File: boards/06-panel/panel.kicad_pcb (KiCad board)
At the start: 2 copper layers, 187 x 219 mm, 229 parts, among them J1 BUS, Q1 2N7000, Q10 2N7000, Q11 2N7000, Q12 2N7000, Q13 2N7000, Q14 2N7000, Q15 2N7000, Q16 2N7000, Q17 2N7000, Q18 2N7000, Q19 2N7000, Q2 2N7000, Q20 2N7000, Q21 2N7000, Q22 2N7000, Q23 2N7000, Q24 2N7000, Q25 2N7000, Q26 2N7000, Q27 2N7000, Q28 2N7000, Q29 2N7000, Q3 2N7000, Q30 2N7000, Q31 2N7000, Q32 2N7000, Q33 2N7000, Q34 2N7000, Q35 2N7000, Q36 2N7000, Q37 2N7000, Q38 2N7000, Q39 2N7000, Q4 2N7000, Q40 2N7000, Q41 2N7000, Q42 2N7000, Q43 2N7000, Q44 2N7000, Q45 2N7000, Q46 2N7000, Q47 2N7000, Q48 2N7000, Q49 2N7000, Q5 2N7000, Q50 2N7000, Q6 2N7000, Q7 2N7000, Q8 2N7000, Q9 2N7000, SW1 A3..A0 B3..B0, SW2 SUB EO AI AO BI BA AB OI, SW3 IO II PCE PCL FI HLT - -, SW4 DATA (closed = 1 on the bus), SW5 CLK, SW6 RST

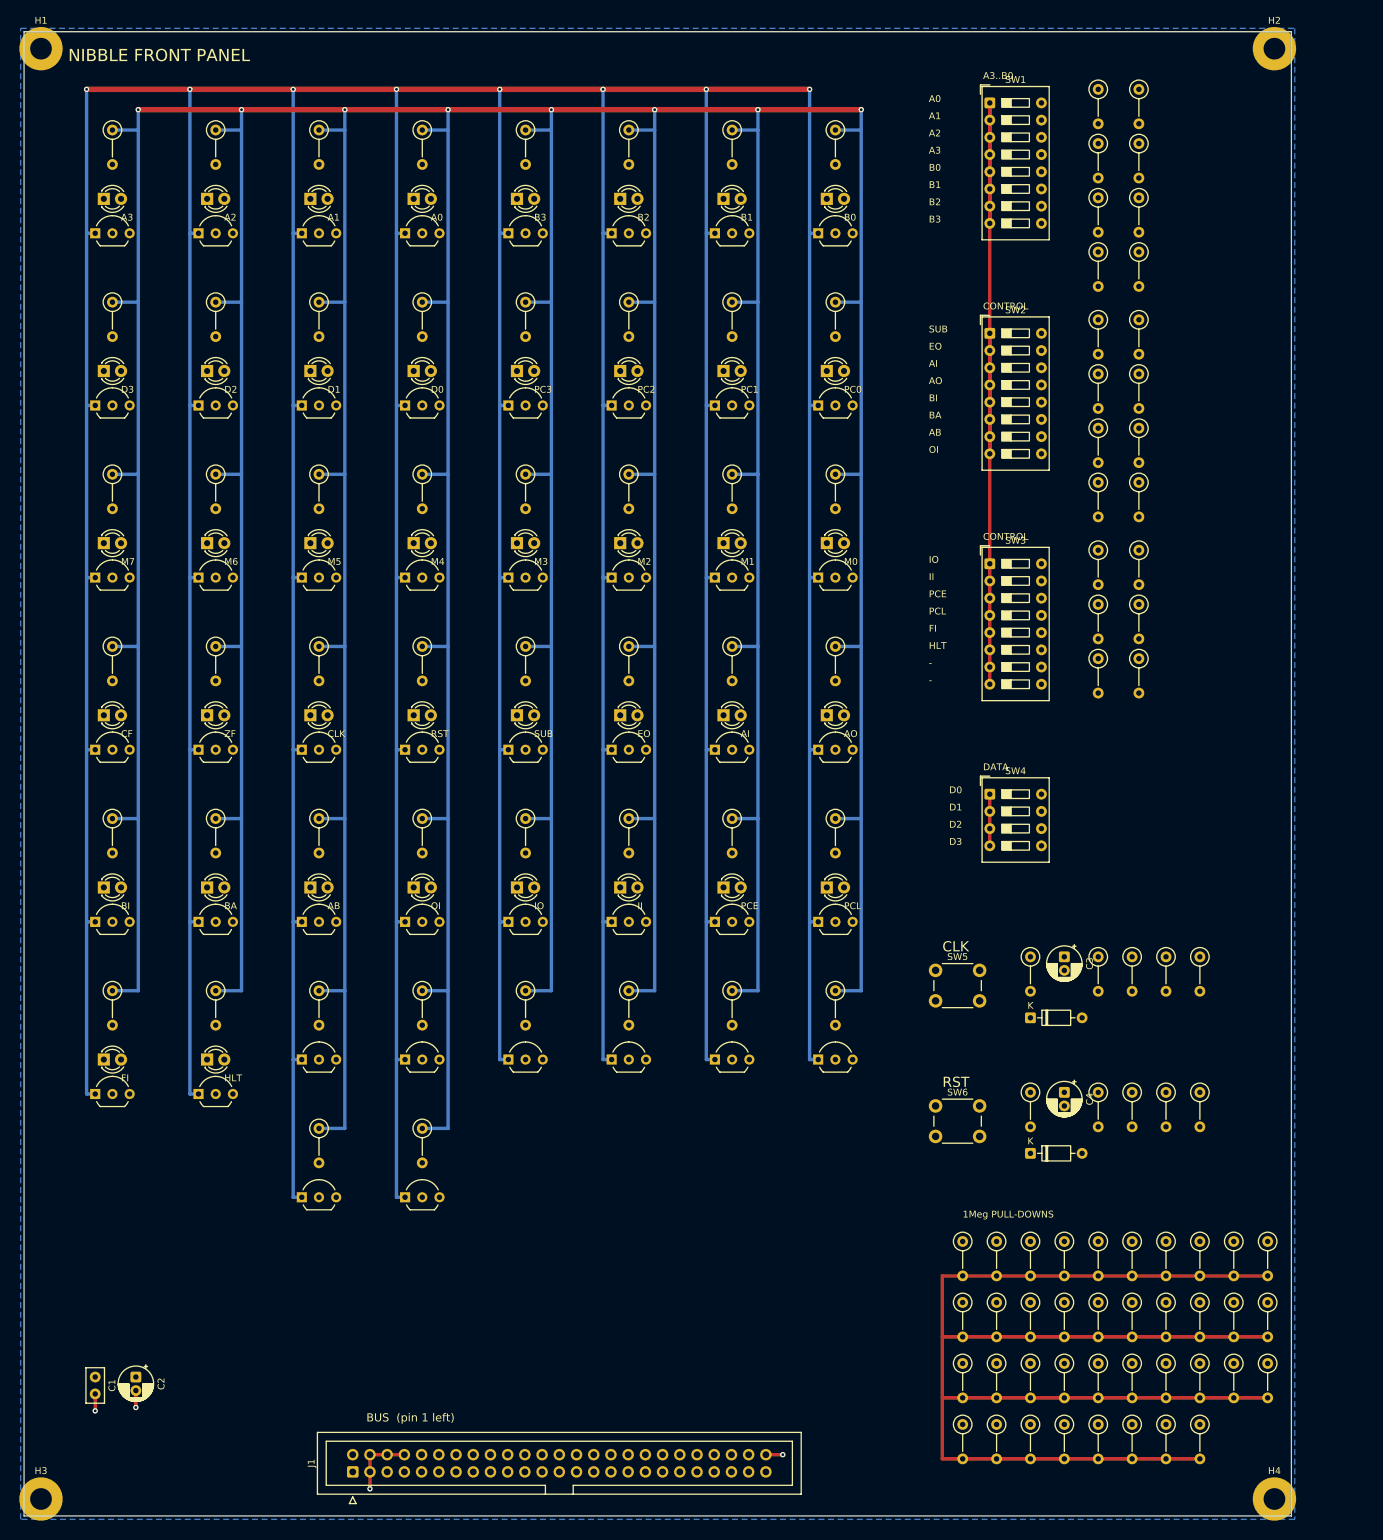
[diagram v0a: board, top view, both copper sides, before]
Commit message: Front panel PCB routed and DRC clean; all four order-1 boards complete
Panel 200x222 mm: LED rows labelled A3..B0 / D3..PC0 / M7..M0 / flags+control,
DIP switches with silk labels, CLK/RST buttons, pull-down grid, header at the
bottom. pcb.py: pre-routed power fixed in the DSN, keep-best across attempts,
DRC-verified ground stitching. Decision D016.

Co-Authored-By: Claude Fable 5.1 <noreply@anthropic.com>
Claude-Session: https://claude.ai/code/session_019vcbW37ERmrjZaWq55Er3J
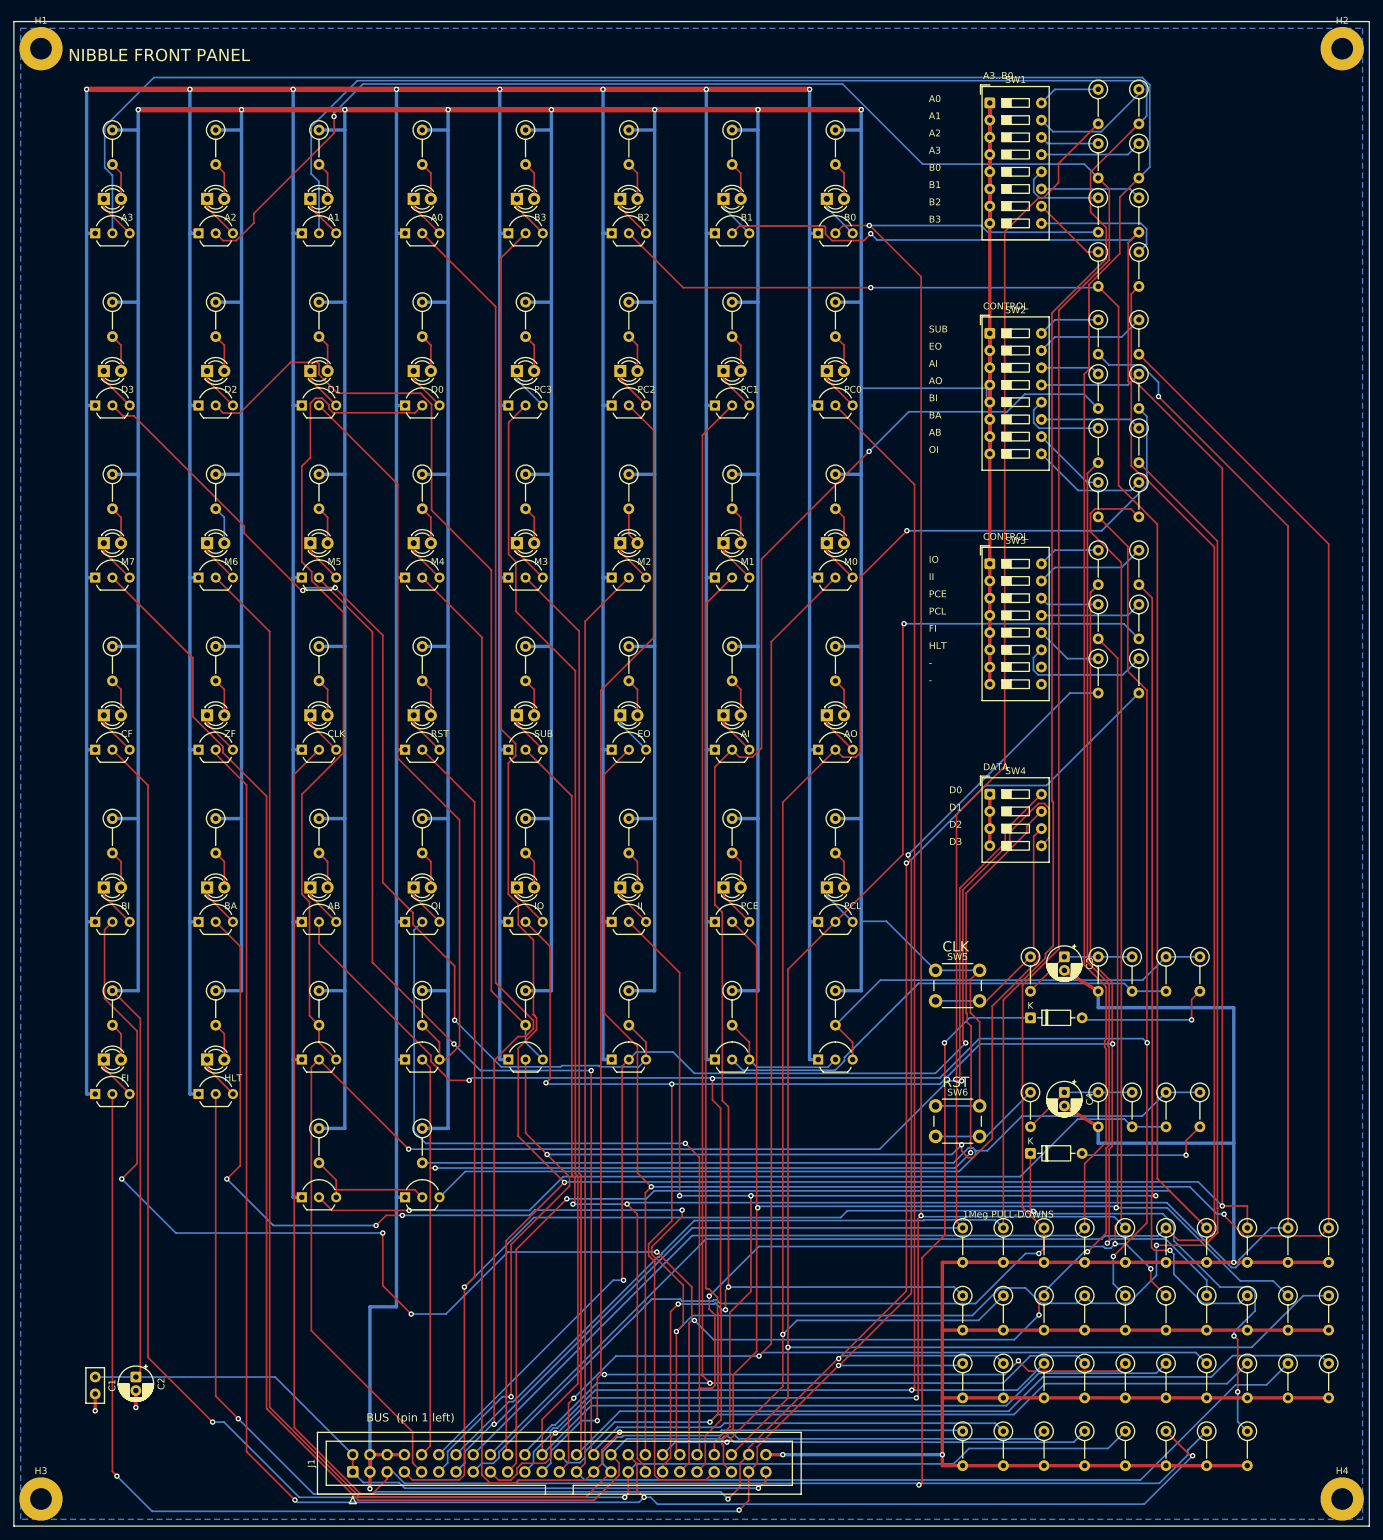
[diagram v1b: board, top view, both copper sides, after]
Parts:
- moved H2 10.0 mm to (196.0, 4.00)
- moved H4 10.0 mm to (196.0, 218.0)
- moved R42 9.22 mm to (194.0, 178.0)
- moved R52 9.06 mm to (194.0, 188.0)
- moved R62 9.00 mm to (194.0, 198.0)
- moved R41 8.25 mm to (188.0, 178.0)
- moved R51 8.06 mm to (188.0, 188.0)
- moved R61 8.00 mm to (188.0, 198.0)
- moved R40 7.28 mm to (182.0, 178.0)
- moved R50 7.07 mm to (182.0, 188.0)
- moved R70 7.07 mm to (182.0, 208.0)
- moved R60 7.00 mm to (182.0, 198.0)
- moved R39 6.32 mm to (176.0, 178.0)
- moved R49 6.08 mm to (176.0, 188.0)
- moved R69 6.08 mm to (176.0, 208.0)
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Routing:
- net A3: track 0.00 -> 453.4 mm
- net A0: track 0.00 -> 448.6 mm, vias 0 -> 1
- net B3: track 0.00 -> 439.9 mm, vias 0 -> 2
- net A1: track 0.00 -> 417.8 mm
- net A2: track 0.00 -> 412.9 mm, vias 0 -> 2
- net SUB: track 0.00 -> 366.5 mm, vias 0 -> 3
- net BA: track 0.00 -> 361.5 mm, vias 0 -> 6
- net B2: track 0.00 -> 359.3 mm, vias 0 -> 2
- net BI: track 0.00 -> 358.6 mm, vias 0 -> 7
- net EO: track 0.00 -> 352.8 mm, vias 0 -> 2
- net B1: track 0.00 -> 339.0 mm, vias 0 -> 1
- net OI: track 0.00 -> 328.0 mm, vias 0 -> 4
- net CLK: track 0.00 -> 327.8 mm, vias 0 -> 2
- net AB: track 0.00 -> 318.1 mm, vias 0 -> 4
- net B0: track 0.00 -> 317.7 mm, vias 0 -> 4
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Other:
- board size 187 x 219 mm -> 200 x 222 mm
